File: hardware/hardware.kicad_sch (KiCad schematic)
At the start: 18 parts, among them Q1 AON6500, Q2 AON6500, Q3 AON6500, Q4 AON6500, Q5 AON6500, Q6 AON6500

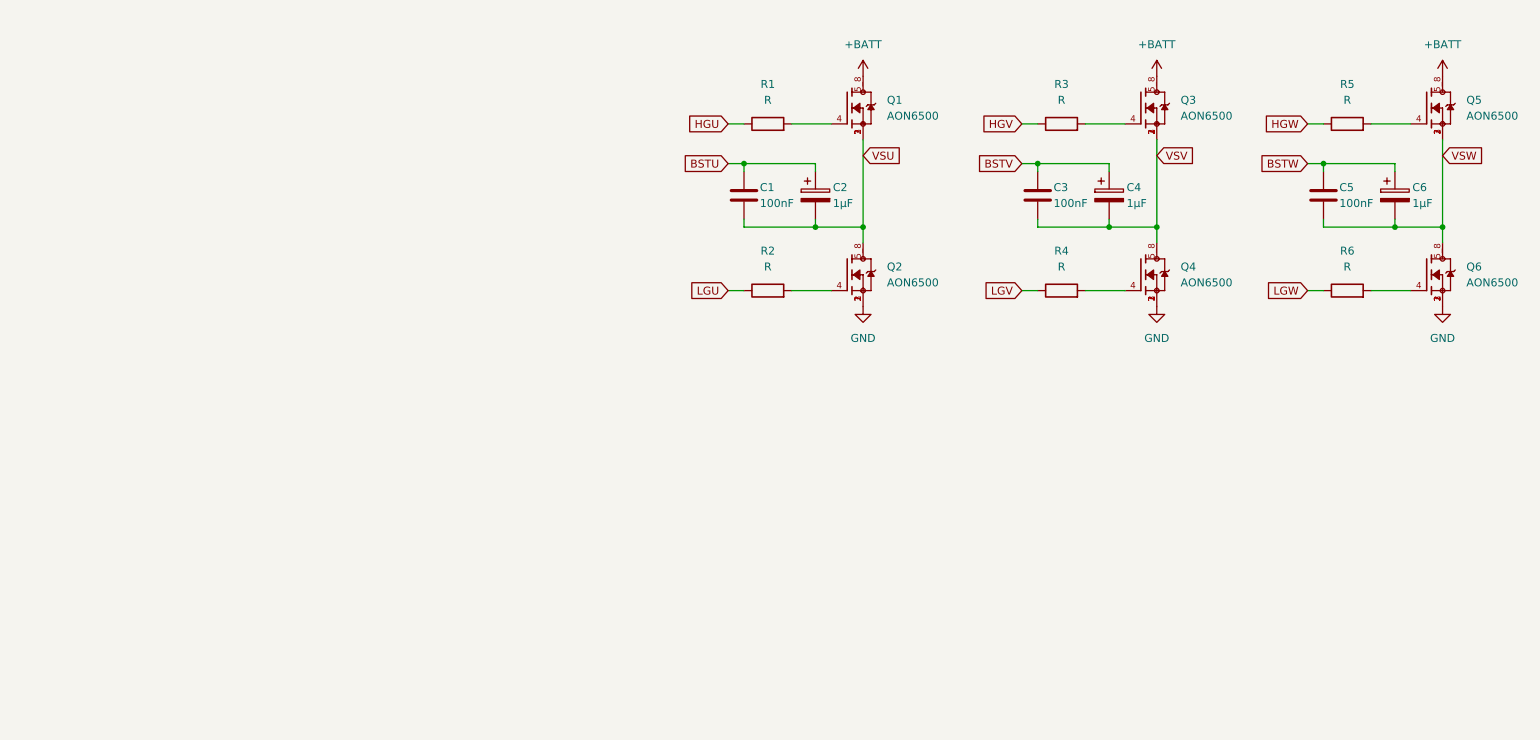
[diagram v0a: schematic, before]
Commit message: wire esc + add minimal connector for ch32m007
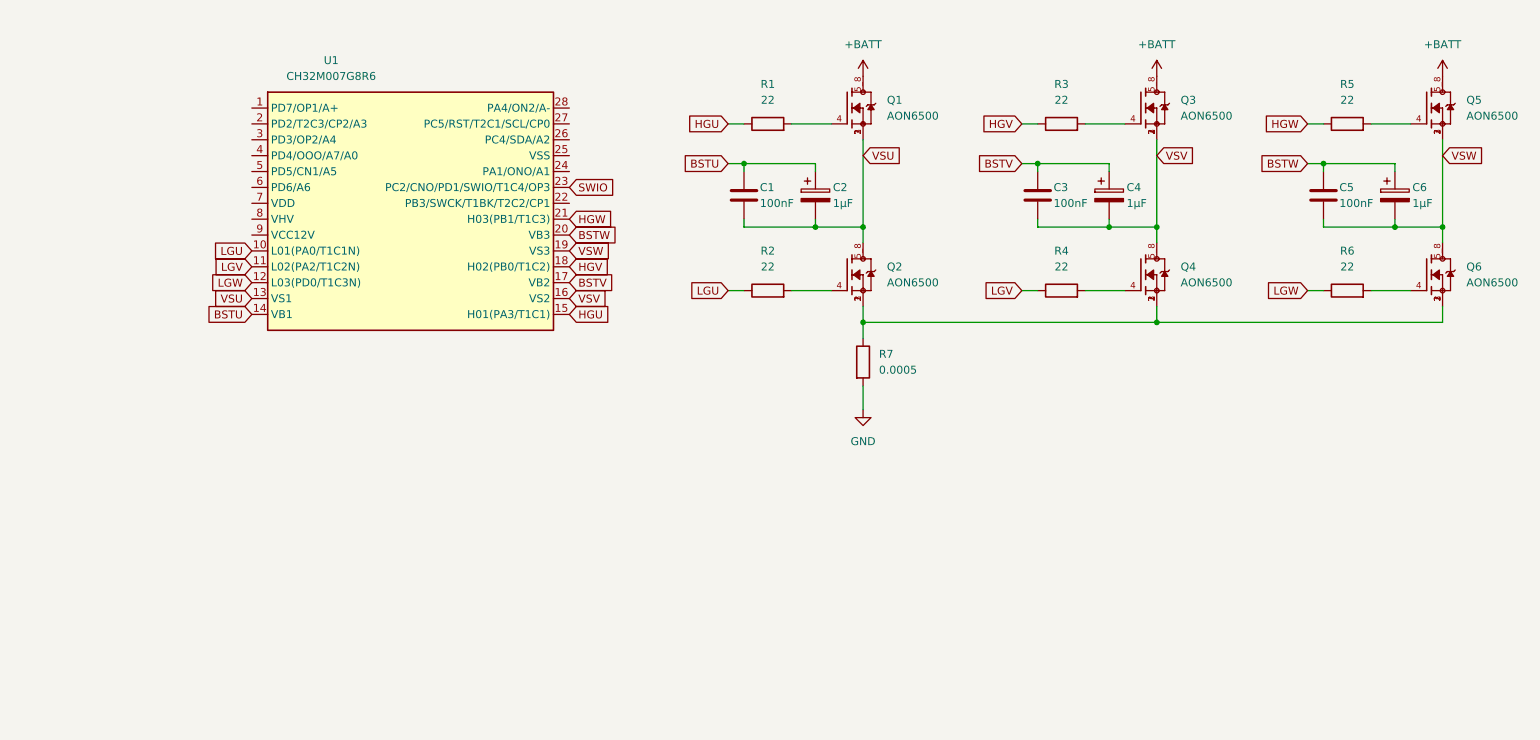
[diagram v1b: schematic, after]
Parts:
- added R7: 0.0005, Resistor_SMD:R_2512_6332Metric, symbol Device:R
- added U1: CH32M007G8R6, Package_SO:TSSOP-28_4.4x9.7mm_P0.65mm, symbol CH32M007G8R6:CH32M007G8R6
- C1, C3, C5: footprint (none) -> Capacitor_SMD:C_1206_3216Metric
- C2, C4, C6: footprint (none) -> Capacitor_SMD:CP_Elec_6.3x3
- R1, R2, R3, R4, R5, R6: value R -> 22; footprint (none) -> Resistor_SMD:R_0603_1608Metric
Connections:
- net BSTU: now also U1.14 (VB1)
- net BSTV: now also U1.17 (VB2)
- net BSTW: now also U1.20 (VB3)
- net GND: now also R7.2; no longer Q2.1, Q2.2, Q2.3, Q4.1, Q4.2, Q4.3, Q6.1, Q6.2, Q6.3
- net HGU: now also U1.15 (H01(PA3/T1C1))
- net HGV: now also U1.18 (H02(PB0/T1C2))
- net HGW: now also U1.21 (H03(PB1/T1C3))
- net LGU: now also U1.10 (L01(PA0/T1C1N))
- net LGV: now also U1.11 (L02(PA2/T1C2N))
- net LGW: now also U1.12 (L03(PD0/T1C3N))
- net VSU: now also U1.13 (VS1)
- net VSV: now also U1.16 (VS2)
- net VSW: now also U1.19 (VS3)
- new net: Q2.1, Q2.2, Q2.3, Q4.1, Q4.2, Q4.3, Q6.1, Q6.2, Q6.3, R7.1
- new net SWIO: U1.23 (PC2/CNO/PD1/SWIO/T1C4/OP3)

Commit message: wire bemf
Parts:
- added R10, R8, R9: 33k, symbol Device:R
- added R11, R12, R13: 5.1k, symbol Device:R
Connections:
- net GND: now also R11.2, R12.2, R13.2
- net VSU: now also R8.1
- net VSV: now also R9.1
- net VSW: now also R10.1
- net OP1: now reaches Q2.1, Q2.2, Q2.3, Q4.1, Q4.2, Q4.3, Q6.1, Q6.2, Q6.3, R7.1
- net OP1: now also U1.1 (PD7/OP1/A+)
- net PD2: now reaches U1.2 (PD2/T2C3/CP2/A3)
- net PD2: now also R13.1, R8.2
- net PA1: now reaches U1.24 (PA1/ONO/A1)
- net PD3: now reaches U1.3 (PD3/OP2/A4)
- net PD3: now also R12.1, R9.2
- net PD4: now reaches U1.4 (PD4/OOO/A7/A0)
- net PD4: now also R10.2, R11.1

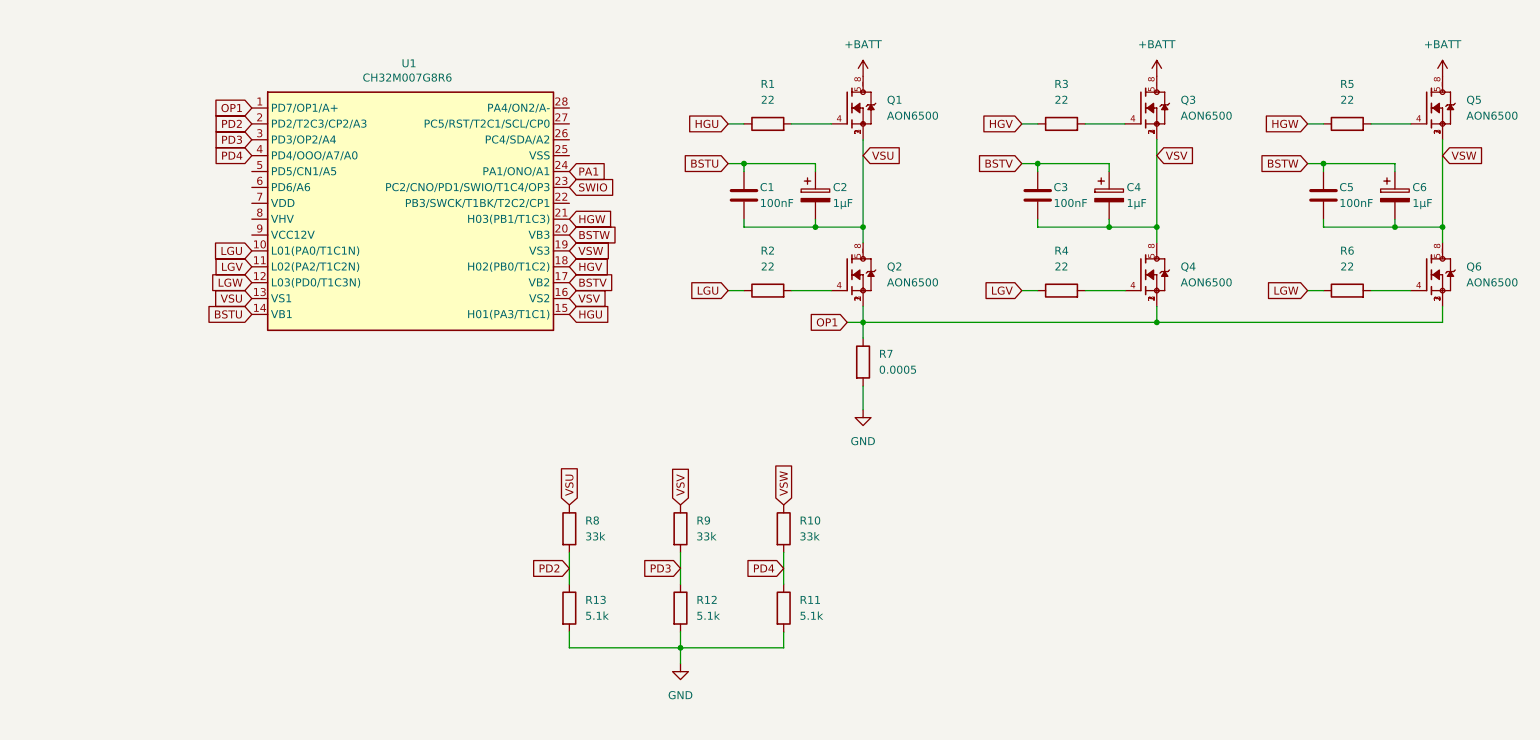
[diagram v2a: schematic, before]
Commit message: add pad gnd and wire drivers with pwm
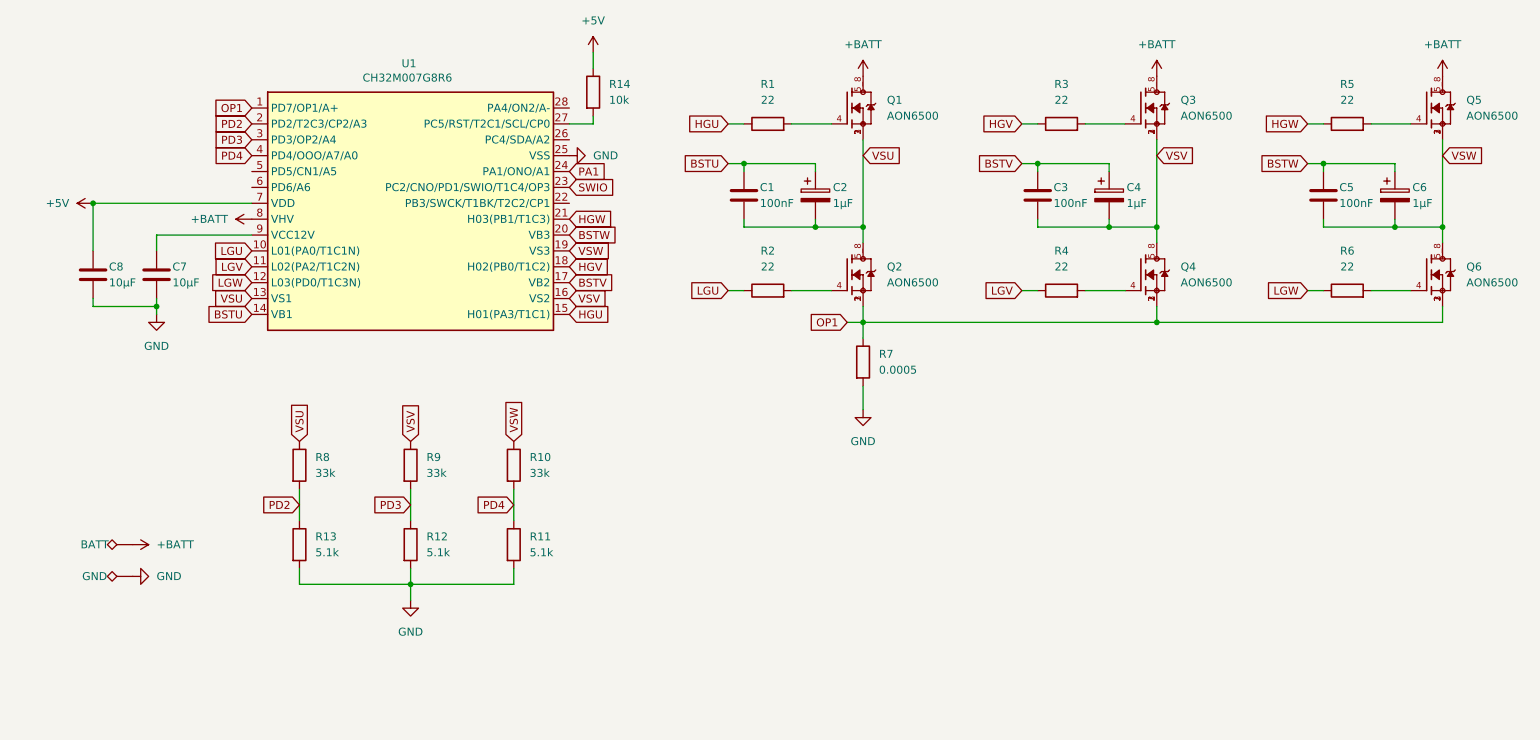
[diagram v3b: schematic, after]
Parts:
- added BATT, GND: TestPoint_Alt, TestPoint:TestPoint_Pad_3.0x3.0mm, symbol Connector:TestPoint_Alt
- added C7, C8: 10µF, Capacitor_SMD:C_1206_3216Metric, symbol Device:C
- added R14: 10k, Resistor_SMD:R_0603_1608Metric, symbol Device:R
- C2, C4, C6: footprint Capacitor_SMD:CP_Elec_6.3x3 -> Capacitor_SMD:CP_Elec_4x4.5
- R10, R11, R12, R13, R8, R9: footprint (none) -> Resistor_SMD:R_0603_1608Metric
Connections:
- net +BATT: now also U1.8 (VHV), BATT.1
- net GND: now also U1.25 (VSS), C7.1, C8.1, GND.1
- net at U1.27 (PC5/RST/T2C1/SCL/CP0): now also R14.2
- net +5V: now reaches U1.7 (VDD)
- net +5V: now also C8.2, R14.1
- net at U1.9 (VCC12V): now also C7.2
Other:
- moved on the sheet: R10, R11, R12, R13, R8, R9

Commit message: finish wire pcb
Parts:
- added J1: Conn_01x02, symbol Connector_Generic:Conn_01x02
- renumbered BATT to BATT1, GND to GND1
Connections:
- net GND: now also J1.1 (Pin_1)
- net PA1: now also J1.2 (Pin_2)
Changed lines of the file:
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@@
 		)
 	)
+	(global_label "PA1"
+		(shape input)
+		(at 25.4 24.13 0)
+		(fields_autoplaced yes)
+		(effects
+			(font
+				(size 1.27 1.27)
+			)
+			(justify left)
+		)
+		(property "Intersheetrefs" "${INTERSHEET_REFS}"
+			(at 31.9533 24.13 0)
+			(effects
+				(font
+					(size 1.27 1.27)
+				)
+				(justify left)
+				(hide yes)
+			)
+		)
+	)
 	(global_label "OP1"
 		(shape input)
@@
 	)
 	(symbol
+		(lib_id "Connector_Generic:Conn_01x02")
+		(at 20.32 26.67 180)
+		(unit 1)
+		(exclude_from_sim no)
+		(in_bom yes)
+		(on_board yes)
+		(dnp no)
+		(fields_autoplaced yes)
+		(property "Reference" "J1"
+			(at 20.32 17.78 0)
+			(effects
+				(font
+					(size 1.27 1.27)
+				)
+			)
+		)
+		(property "Value" "Conn_01x02"
+			(at 20.32 20.32 0)
+			(effects
+				(font
+					(size 1.27 1.27)
+				)
+			)
+		)
+		(property "Footprint" ""
+			(at 20.32 26.67 0)
+			(effects
+				(font
+					(size 1.27 1.27)
+				)
+				(hide yes)
+			)
+		)
+		(property "Datasheet" "~"
+			(at 20.32 26.67 0)
+			(effects
+				(font
+					(size 1.27 1.27)
+				)
+				(hide yes)
+			)
+		)
+		(property "Description" "Generic connector, single row, 01x02, script generated (kicad-library-utils/schlib/autogen/connector/)"
+			(at 20.32 26.67 0)
+			(effects
+				(font
+					(size 1.27 1.27)
+				)
+				(hide yes)
+			)
+		)
+		(pin "2"
+		)
+		(pin "1"
+		)
+		(instances
+			(project ""
+				(path "/8190213a-0743-4626-9b51-f7fca6052b18"
+					(reference "J1")
+					(unit 1)
+				)
+			)
+		)
+	)
+	(symbol
 		(lib_id "power:+5V")
 		(at 106.68 19.05 0)
@@
 		(on_board yes)
 		(dnp no)
-		(property "Reference" "GND"
+		(property "Reference" "GND1"
 			(at 26.924 102.87 90)
 			(effects
@@
 			(project "hardware"
 				(path "/8190213a-0743-4626-9b51-f7fca6052b18"
-					(reference "GND")
+					(reference "GND1")
 					(unit 1)
 				)
@@
 		(on_board yes)
 		(dnp no)
-		(property "Reference" "BATT"
+		(property "Reference" "BATT1"
 			(at 26.924 97.79 90)
 			(effects
@@
 			(project ""
 				(path "/8190213a-0743-4626-9b51-f7fca6052b18"
-					(reference "BATT")
+					(reference "BATT1")
 					(unit 1)
 				)
@@
 					(unit 1)
 				)
+			)
+		)
+	)
+	(symbol
+		(lib_id "power:GND")
+		(at 25.4 26.67 90)
+		(unit 1)
+		(exclude_from_sim no)
+		(in_bom yes)
+		(on_board yes)
+		(dnp no)
+		(fields_autoplaced yes)
+		(property "Reference" "#PWR011"
+			(at 31.75 26.67 0)
+			(effects
+				(font
+					(size 1.27 1.27)
+				)
+				(hide yes)
+			)
+		)
+		(property "Value" "GND"
+			(at 29.21 26.6699 90)
+			(effects
+				(font
+					(size 1.27 1.27)
+				)
+				(justify right)
+			)
+		)
+		(property "Footprint" ""
+			(at 25.4 26.67 0)
+			(effects
+				(font
+					(size 1.27 1.27)
+				)
+				(hide yes)
+			)
+		)
+		(property "Datasheet" ""
+			(at 25.4 26.67 0)
+			(effects
+				(font
+					(size 1.27 1.27)
+				)
+				(hide yes)
+			)
+		)
+		(property "Description" "Power symbol creates a global label with name \"GND\" , ground"
+			(at 25.4 26.67 0)
+			(effects
+				(font
+					(size 1.27 1.27)
+				)
+				(hide yes)
+			)
+		)
+		(pin "1"
+		)
+		(instances
+			(project "hardware"
+				(path "/8190213a-0743-4626-9b51-f7fca6052b18"
+					(reference "#PWR011")
+					(unit 1)
+				)

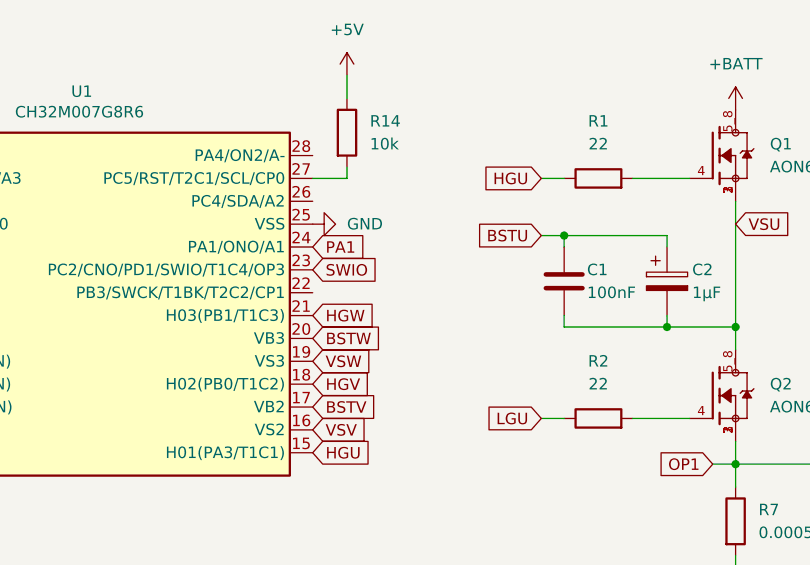
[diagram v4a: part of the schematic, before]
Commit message: add programming pad
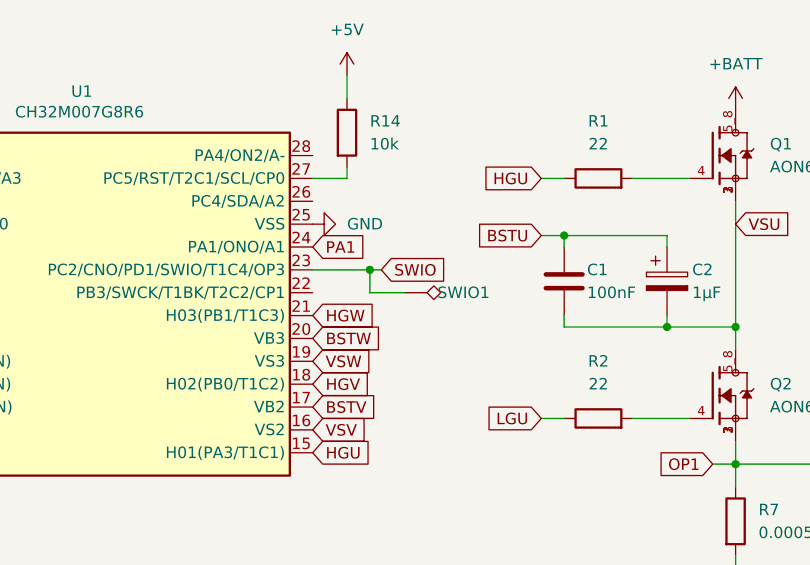
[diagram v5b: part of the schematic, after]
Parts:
- added SWIO1: TestPoint_Alt, TestPoint:TestPoint_Pad_1.5x1.5mm, symbol Connector:TestPoint_Alt
- J1: footprint (none) -> Connector_PinHeader_2.54mm:PinHeader_1x02_P2.54mm_Vertical
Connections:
- net SWIO: now also SWIO1.1
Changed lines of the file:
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@@
+	)
+	(junction
+		(at 109.22 40.64)
+		(diameter 0)
+		(color 0 0 0 0)
 	)
 	(junction
@@
 	(wire
 		(pts
+			(xy 109.22 43.18) (xy 109.22 40.64)
+		)
+		(stroke
+			(width 0)
+			(type default)
+		)
+	)
+	(wire
+		(pts
 			(xy 93.98 88.9) (xy 93.98 93.98)
 		)
@@
 	(wire
 		(pts
+			(xy 109.22 40.64) (xy 102.87 40.64)
+		)
+		(stroke
+			(width 0)
+			(type default)
+		)
+	)
+	(wire
+		(pts
 			(xy 196.85 62.23) (xy 242.57 62.23)
 		)
@@
 	(wire
 		(pts
+			(xy 110.49 40.64) (xy 109.22 40.64)
+		)
+		(stroke
+			(width 0)
+			(type default)
+		)
+	)
+	(wire
+		(pts
 			(xy 149.86 62.23) (xy 149.86 64.77)
 		)
@@
 		)
 	)
+	(wire
+		(pts
+			(xy 113.03 43.18) (xy 109.22 43.18)
+		)
+		(stroke
+			(width 0)
+			(type default)
+		)
+	)
 	(global_label "VSW"
 		(shape input)
@@
 	(global_label "SWIO"
 		(shape input)
-		(at 102.87 40.64 0)
+		(at 110.49 40.64 0)
 		(fields_autoplaced yes)
 		(effects
@@
 		)
 		(property "Intersheetrefs" "${INTERSHEET_REFS}"
-			(at 110.4514 40.64 0)
+			(at 118.0714 40.64 0)
 			(effects
 				(font
@@
 	)
 	(symbol
+		(lib_id "Connector:TestPoint_Alt")
+		(at 113.03 43.18 270)
+		(unit 1)
+		(exclude_from_sim no)
+		(in_bom yes)
+		(on_board yes)
+		(dnp no)
+		(property "Reference" "SWIO1"
+			(at 119.634 43.18 90)
+			(effects
+				(font
+					(size 1.27 1.27)
+				)
+			)
+		)
+		(property "Value" "TestPoint_Alt"
+			(at 116.332 45.72 90)
+			(effects
+				(font
+					(size 1.27 1.27)
+				)
+				(hide yes)
+			)
+		)
+		(property "Footprint" "TestPoint:TestPoint_Pad_1.5x1.5mm"
+			(at 113.03 48.26 0)
+			(effects
+				(font
+					(size 1.27 1.27)
+				)
+				(hide yes)
+			)
+		)
+		(property "Datasheet" "~"
+			(at 113.03 48.26 0)
+			(effects
+				(font
+					(size 1.27 1.27)
+				)
+				(hide yes)
+			)
+		)
+		(property "Description" "test point (alternative shape)"
+			(at 113.03 43.18 0)
+			(effects
+				(font
+					(size 1.27 1.27)
+				)
+				(hide yes)
+			)
+		)
+		(pin "1"
+		)
+		(instances
+			(project "hardware"
+				(path "/8190213a-0743-4626-9b51-f7fca6052b18"
+					(reference "SWIO1")
+					(unit 1)
+				)
+			)
+		)
+	)
+	(symbol
 		(lib_id "Device:C_Polarized")
 		(at 234.95 41.91 0)
@@
 			)
 		)
-		(property "Footprint" ""
+		(property "Footprint" "Connector_PinHeader_2.54mm:PinHeader_1x02_P2.54mm_Vertical"
 			(at 20.32 26.67 0)
 			(effects

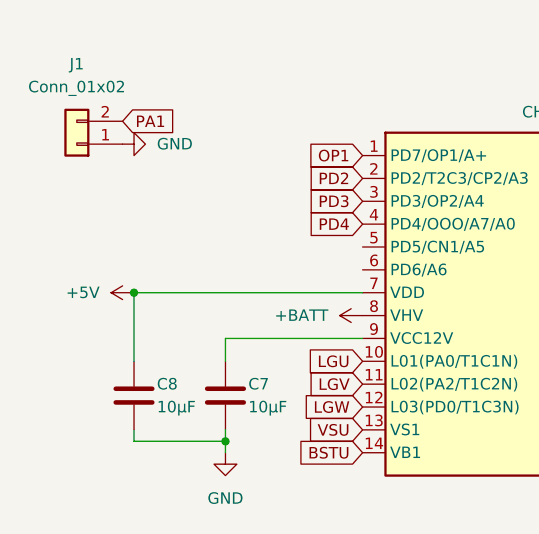
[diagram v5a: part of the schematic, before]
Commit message: add 3.3v connection
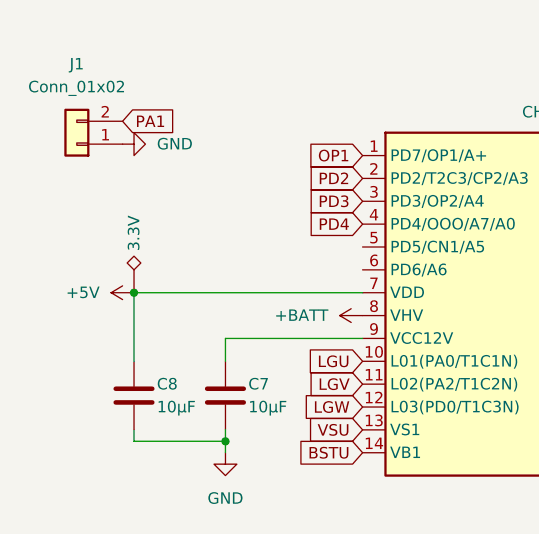
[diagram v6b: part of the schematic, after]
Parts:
- added 3.3V: TestPoint_Alt, TestPoint:TestPoint_Pad_1.5x1.5mm, symbol Connector:TestPoint_Alt
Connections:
- net +5V: now also 3.3V.1
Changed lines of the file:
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@@
+	)
+	(symbol
+		(lib_id "Connector:TestPoint_Alt")
+		(at 26.67 43.18 0)
+		(unit 1)
+		(exclude_from_sim no)
+		(in_bom yes)
+		(on_board yes)
+		(dnp no)
+		(property "Reference" "3.3V"
+			(at 26.67 36.576 90)
+			(effects
+				(font
+					(size 1.27 1.27)
+				)
+			)
+		)
+		(property "Value" "TestPoint_Alt"
+			(at 29.21 39.878 90)
+			(effects
+				(font
+					(size 1.27 1.27)
+				)
+				(hide yes)
+			)
+		)
+		(property "Footprint" "TestPoint:TestPoint_Pad_1.5x1.5mm"
+			(at 31.75 43.18 0)
+			(effects
+				(font
+					(size 1.27 1.27)
+				)
+				(hide yes)
+			)
+		)
+		(property "Datasheet" "~"
+			(at 31.75 43.18 0)
+			(effects
+				(font
+					(size 1.27 1.27)
+				)
+				(hide yes)
+			)
+		)
+		(property "Description" "test point (alternative shape)"
+			(at 26.67 43.18 0)
+			(effects
+				(font
+					(size 1.27 1.27)
+				)
+				(hide yes)
+			)
+		)
+		(pin "1"
+		)
+		(instances
+			(project "hardware"
+				(path "/8190213a-0743-4626-9b51-f7fca6052b18"
+					(reference "3.3V")
+					(unit 1)
+				)
+			)
+		)
 	)
 	(symbol
